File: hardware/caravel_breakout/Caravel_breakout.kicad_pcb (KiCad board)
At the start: 2 copper layers, 25.4 x 25.4 mm, 18 parts, among them J1 Conn_01x14_Female, J2 Conn_01x14_Female, J3 Conn_01x14_Female, J4 Conn_01x14_Female, T1 Logo, T2 Logo, U1 Caravel

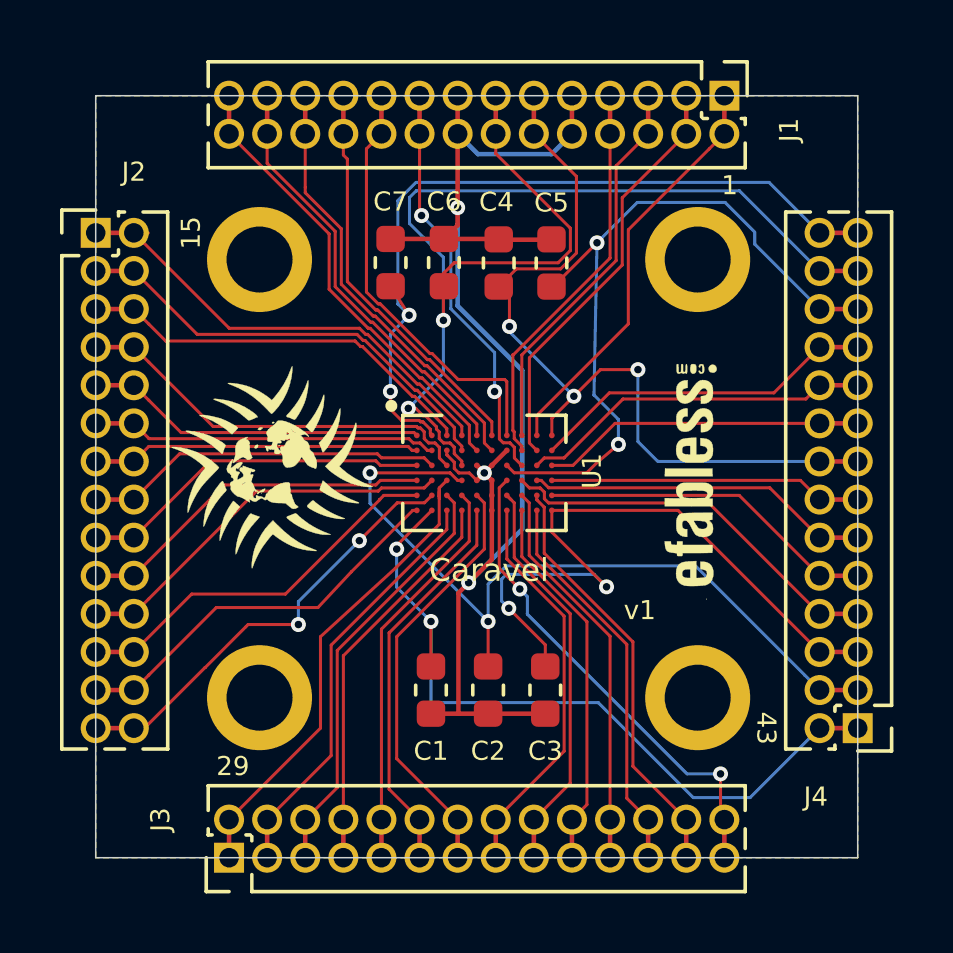
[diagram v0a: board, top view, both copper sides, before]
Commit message: Update caravel breakout PCB
Switches to smaller passives.
Moves passives closer to the IC pads.
Increases the width of the power traces.
Decreases the clearance on the PCB pours.
Tweaks the silkscreen as needed.

Signed-off-by: Michael Welling <mwelling@ieee.org>
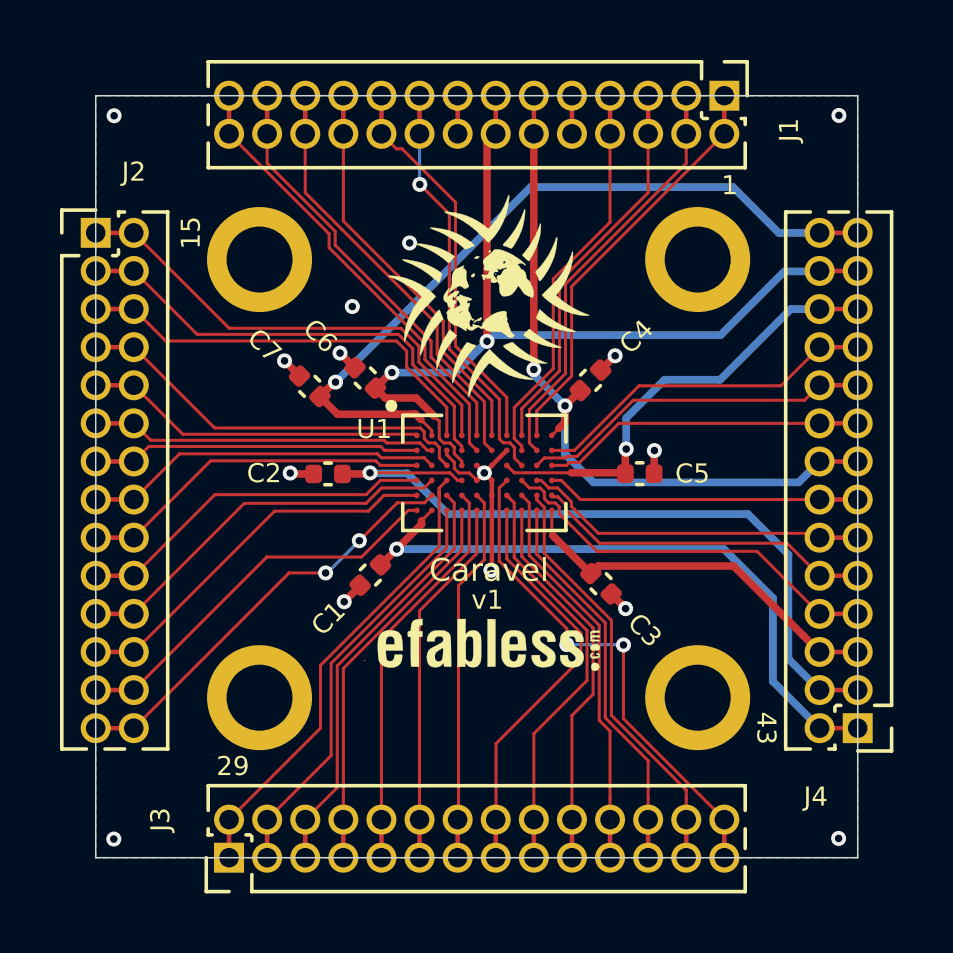
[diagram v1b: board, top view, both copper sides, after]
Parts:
- C1, C2, C3, C4, C5, C6, C7: footprint Capacitor_SMD:C_0603_1608Metric -> Capacitor_SMD:C_0402_1005Metric
- moved T1 9.20 mm to (136.0, 87.5)
- moved C2 8.97 mm to (130.7, 93.4), turned to 180 degrees
- moved T2 8.80 mm to (136.0, 99.1), turned to 0 degrees
- moved C5 7.61 mm to (141.1, 93.4), turned to 180 degrees
- moved C4 4.97 mm to (139.4, 90.3), turned to 225 degrees
- moved C7 4.93 mm to (130.1, 90.5), turned to 315 degrees
- moved C6 4.66 mm to (131.9, 90.2), turned to 315 degrees
- moved C1 4.33 mm to (132.1, 96.8), turned to 45 degrees
- moved C3 4.00 mm to (139.8, 97.0), turned to 315 degrees
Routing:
- net GND: track 45.5 -> 14.0 mm, vias 3 -> 15
- net vdda2: track 24.1 -> 14.9 mm, vias 2 -> 1
- net vddio: track 39.0 -> 30.4 mm
- net vdda: track 22.5 -> 14.4 mm, vias 2 -> 0
- net vccd1: track 25.2 -> 21.8 mm, vias 2 -> 1
- net vccd: track 27.3 -> 24.3 mm, vias 3 -> 2
- net mprj_io[7]: track 14.0 -> 12.3 mm
- net vdda1: track 26.6 -> 25.2 mm, vias 2 -> 1
- net mprj_io[32]: track 14.3 -> 13.0 mm
- net mprj_io[8]: track 13.0 -> 12.2 mm
- net vccd2: track 26.4 -> 25.6 mm, vias 2 -> 1
- net mprj_io[26]: track 14.8 -> 15.5 mm
- net mprj_io[25]: track 13.4 -> 14.1 mm
- net mprj_io[33]: track 13.7 -> 14.0 mm, vias 2 -> 1
